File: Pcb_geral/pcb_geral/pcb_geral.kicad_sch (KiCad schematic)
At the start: 30 parts, among them U1 LM2594M-3.3, U2 LM2596S-5, U3 STM32F103C6Tx

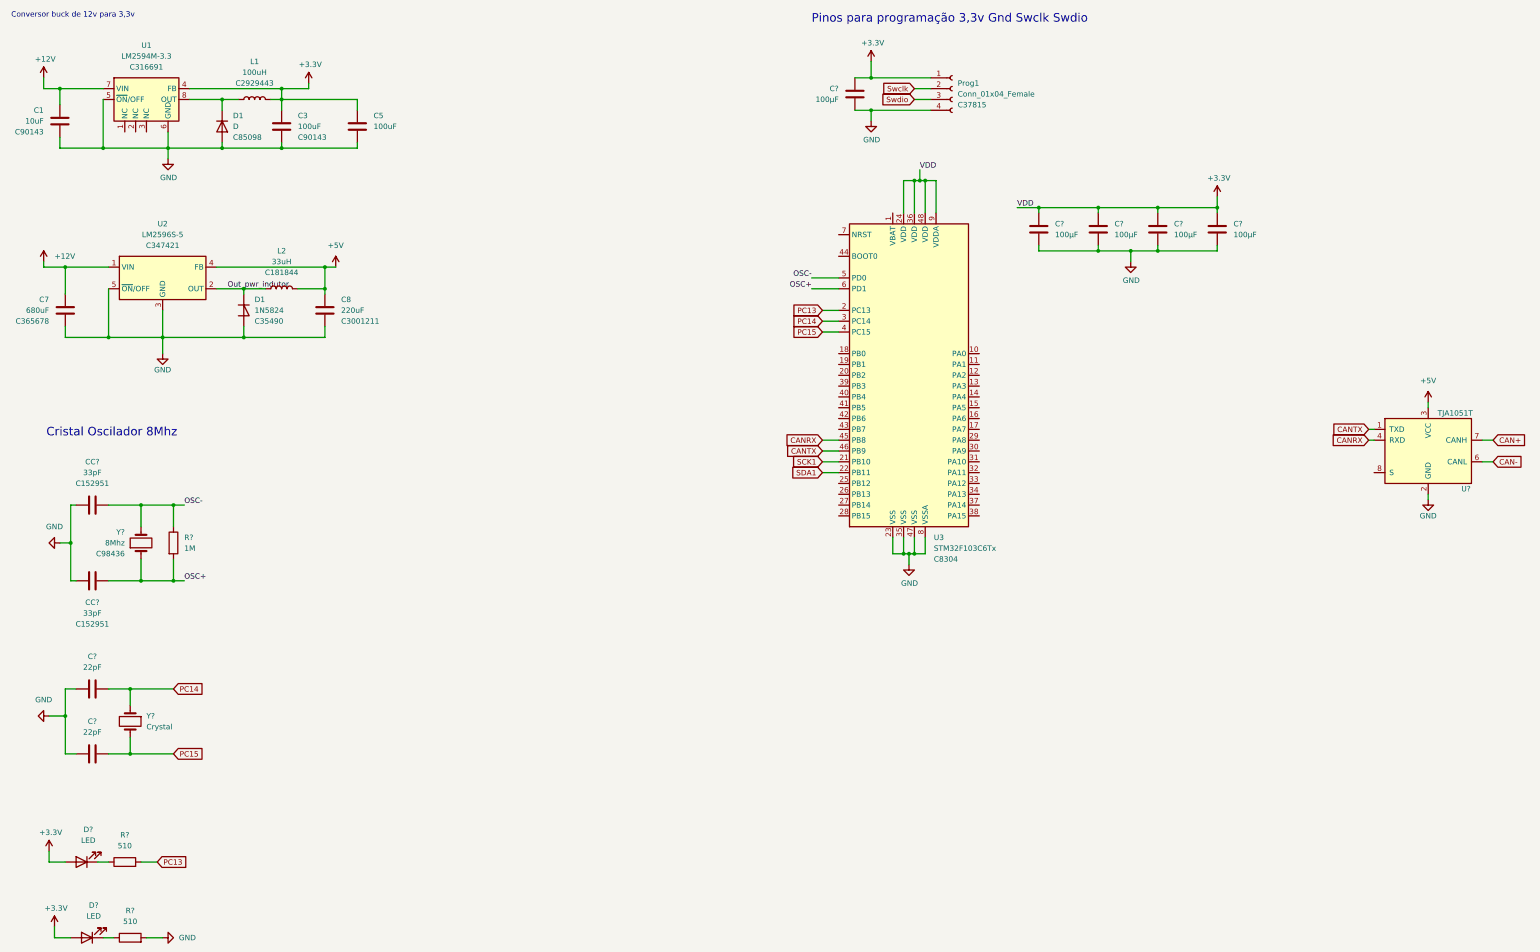
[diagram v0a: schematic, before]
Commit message: cristal clock posicionado, seguindo as boas praticas de desenho de PCI
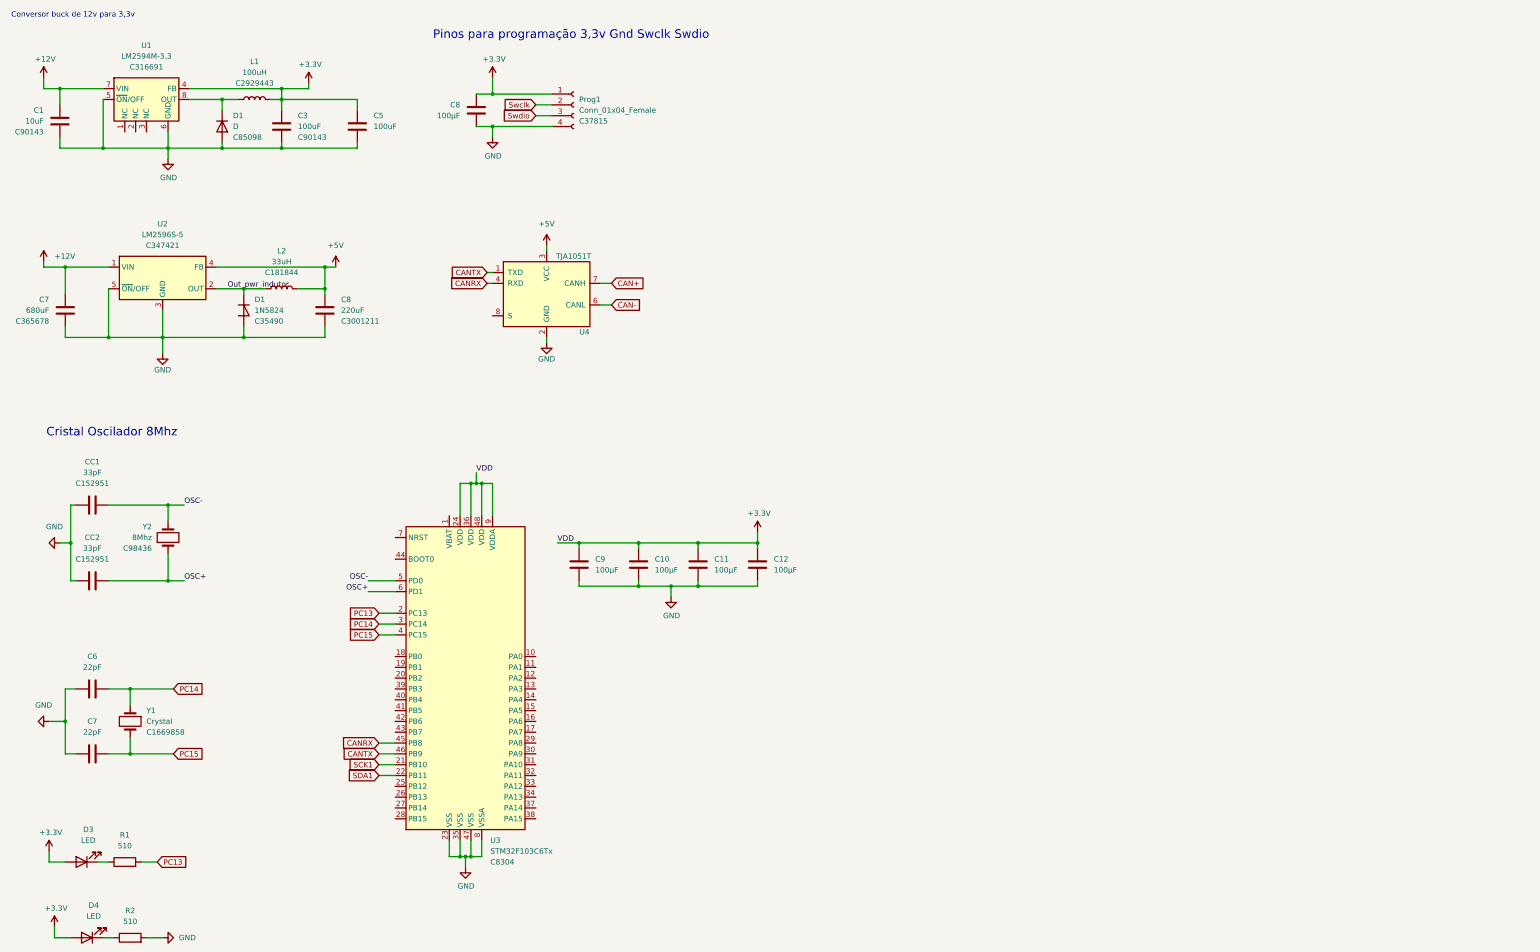
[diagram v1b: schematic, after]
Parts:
- removed R?: 1M, symbol Device:R
- C6, C7: renamed from C?; footprint (none) -> Capacitor_SMD:C_0402_1005Metric
- CC1, CC2: renamed from CC?; footprint Capacitor_SMD:C_1206_3216Metric -> Capacitor_SMD:C_0402_1005Metric
- Y1: renamed from Y?; footprint (none) -> Crystal:Crystal_SMD_3215-2Pin_3.2x1.5mm; LCSC (none) -> C1669858
- gave numbers to parts that had none: 11
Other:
- moved on the sheet: C10, C11, C12, C8, C9, Prog1, U3, U4, Y2

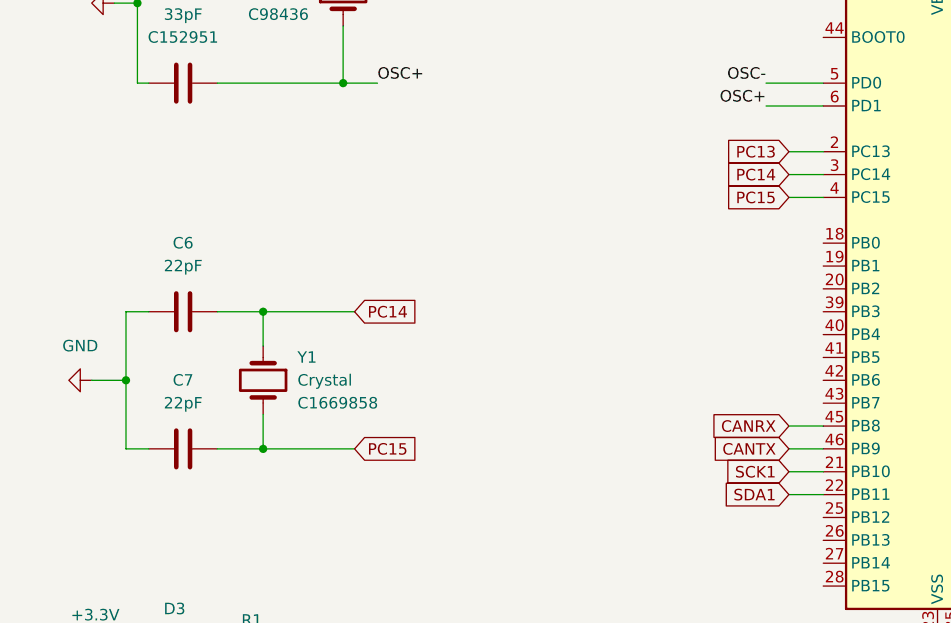
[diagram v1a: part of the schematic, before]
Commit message: plano de alimentação, saparar dos planos alimentação do plano digital
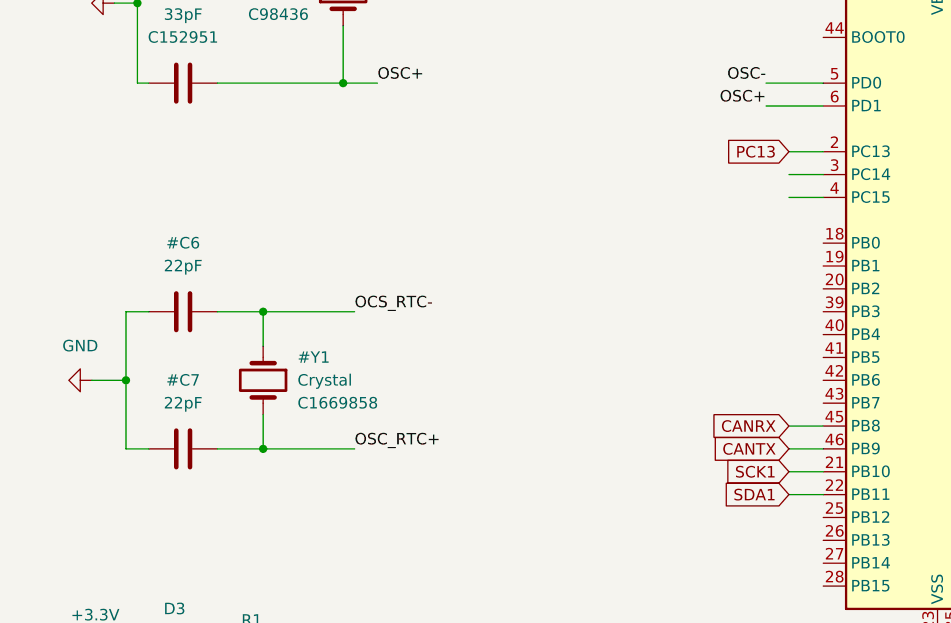
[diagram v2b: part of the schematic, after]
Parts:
- renumbered C6 to #C6, C7 to #C7, Y1 to #Y1
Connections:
- net PC14 renamed OCS_RTC-
- net OCS_RTC-: no longer U3.3 (PC14)
- net PC15 renamed OSC_RTC+
- net OSC_RTC+: no longer U3.4 (PC15)
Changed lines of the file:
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@@
+    (effects (font (size 1.27 1.27)) (justify left bottom))
+  )
+  (label "OSC_RTC+" (at 57.15 194.31 0)
+    (effects (font (size 1.27 1.27)) (justify left bottom))
+  )
+  (label "OCS_RTC-" (at 57.15 179.07 0)
     (effects (font (size 1.27 1.27)) (justify left bottom))
   )
@@
     (property "Intersheet References" "${INTERSHEET_REFS}" (id 0) (at -198.12 -86.36 0)
       (effects (font (size 1.27 1.27)) hide)
-    )
-  )
-  (global_label "PC14" (shape input) (at 105.41 163.83 180) (fields_autoplaced)
-    (effects (font (size 1.27 1.27)) (justify right))
-    (property "Referências entre as folhas" "${INTERSHEET_REFS}" (id 0) (at 98.0379 163.9094 0)
-      (effects (font (size 1.27 1.27)) (justify right) hide)
     )
   )
@@
     )
   )
-  (global_label "PC14" (shape input) (at 57.15 179.07 0) (fields_autoplaced)
-    (effects (font (size 1.27 1.27)) (justify left))
-    (property "Referências entre as folhas" "${INTERSHEET_REFS}" (id 0) (at 64.5221 178.9906 0)
-      (effects (font (size 1.27 1.27)) (justify left) hide)
-    )
-  )
-  (global_label "PC15" (shape input) (at 105.41 166.37 180) (fields_autoplaced)
-    (effects (font (size 1.27 1.27)) (justify right))
-    (property "Referências entre as folhas" "${INTERSHEET_REFS}" (id 0) (at 98.0379 166.4494 0)
-      (effects (font (size 1.27 1.27)) (justify right) hide)
-    )
-  )
   (global_label "CANRX" (shape input) (at 105.41 191.77 180) (fields_autoplaced)
     (effects (font (size 1.27 1.27)) (justify right))
@@
     (effects (font (size 1.27 1.27)) (justify left))
     (property "Referências entre as folhas" "${INTERSHEET_REFS}" (id 0) (at 167.6945 88.8206 0)
-      (effects (font (size 1.27 1.27)) (justify left) hide)
-    )
-  )
-  (global_label "PC15" (shape input) (at 57.15 194.31 0) (fields_autoplaced)
-    (effects (font (size 1.27 1.27)) (justify left))
-    (property "Referências entre as folhas" "${INTERSHEET_REFS}" (id 0) (at 64.5221 194.2306 0)
       (effects (font (size 1.27 1.27)) (justify left) hide)
     )
@@
   (symbol (lib_id "Device:C") (at 38.1 179.07 270) (unit 1)
     (in_bom yes) (on_board yes) (fields_autoplaced)
-    (property "Reference" "C6" (id 0) (at 38.1 171.45 90))
+    (property "Reference" "#C6" (id 0) (at 38.1 171.45 90))
     (property "Value" "22pF" (id 1) (at 38.1 173.99 90))
     (property "Footprint" "Capacitor_SMD:C_0402_1005Metric" (id 2) (at 34.29 180.0352 0)
@@
   (symbol (lib_id "Device:C") (at 38.1 194.31 90) (unit 1)
     (in_bom yes) (on_board yes) (fields_autoplaced)
-    (property "Reference" "C7" (id 0) (at 38.1 186.69 90))
+    (property "Reference" "#C7" (id 0) (at 38.1 186.69 90))
     (property "Value" "22pF" (id 1) (at 38.1 189.23 90))
     (property "Footprint" "Capacitor_SMD:C_0402_1005Metric" (id 2) (at 41.91 193.3448 0)
@@
   (symbol (lib_id "Device:Crystal") (at 46.99 186.69 270) (unit 1)
     (in_bom yes) (on_board yes) (fields_autoplaced)
-    (property "Reference" "Y1" (id 0) (at 50.8 184.1499 90)
+    (property "Reference" "#Y1" (id 0) (at 50.8 184.1499 90)
       (effects (font (size 1.27 1.27)) (justify left))
     )
@@
   )
   (symbol_instances
+    (path "/3c3b178e-c616-4ea7-8f30-c66e0c950bf0"
+      (reference "#C6") (unit 1) (value "22pF") (footprint "Capacitor_SMD:C_0402_1005Metric")
+    )
+    (path "/7be2e455-6634-4ab4-a09f-3f20490326d3"
+      (reference "#C7") (unit 1) (value "22pF") (footprint "Capacitor_SMD:C_0402_1005Metric")
+    )
     (path "/39012e94-5ef2-402d-aee8-2f1ffd09b894"
       (reference "#PWR0101") (unit 1) (value "+12V") (footprint "")
@@
       (reference "#PWR0118") (unit 1) (value "GND") (footprint "")
     )
+    (path "/da12ae5c-eaa8-41ad-a68d-e21ab2de3f4f"
+      (reference "#Y1") (unit 1) (value "Crystal") (footprint "Crystal:Crystal_SMD_3215-2Pin_3.2x1.5mm")
+    )
     (path "/eb52bd06-71f9-42f6-b7ab-65eb78ed70ff"
       (reference "C1") (unit 1) (value "10uF") (footprint "Capacitor_SMD:C_1210_3225Metric")
@@
       (reference "C5") (unit 1) (value "100uF") (footprint "Capacitor_SMD:C_1210_3225Metric")
     )
-    (path "/3c3b178e-c616-4ea7-8f30-c66e0c950bf0"
-      (reference "C6") (unit 1) (value "22pF") (footprint "Capacitor_SMD:C_0402_1005Metric")
-    )
-    (path "/7be2e455-6634-4ab4-a09f-3f20490326d3"
-      (reference "C7") (unit 1) (value "22pF") (footprint "Capacitor_SMD:C_0402_1005Metric")
-    )
     (path "/7cfba9ce-67ff-4188-96f1-3eef539508d4"
       (reference "C8") (unit 1) (value "100µF") (footprint "")
@@
       (reference "U4") (unit 1) (value "TJA1051T") (footprint "Package_SO:SOIC-8_3.9x4.9mm_P1.27mm")
     )
-    (path "/da12ae5c-eaa8-41ad-a68d-e21ab2de3f4f"
-      (reference "Y1") (unit 1) (value "Crystal") (footprint "Crystal:Crystal_SMD_3215-2Pin_3.2x1.5mm")
-    )
     (path "/f904ebcc-aff9-4c26-bd0a-652997ad2e22"
